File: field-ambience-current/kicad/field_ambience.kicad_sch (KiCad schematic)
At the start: 0 parts

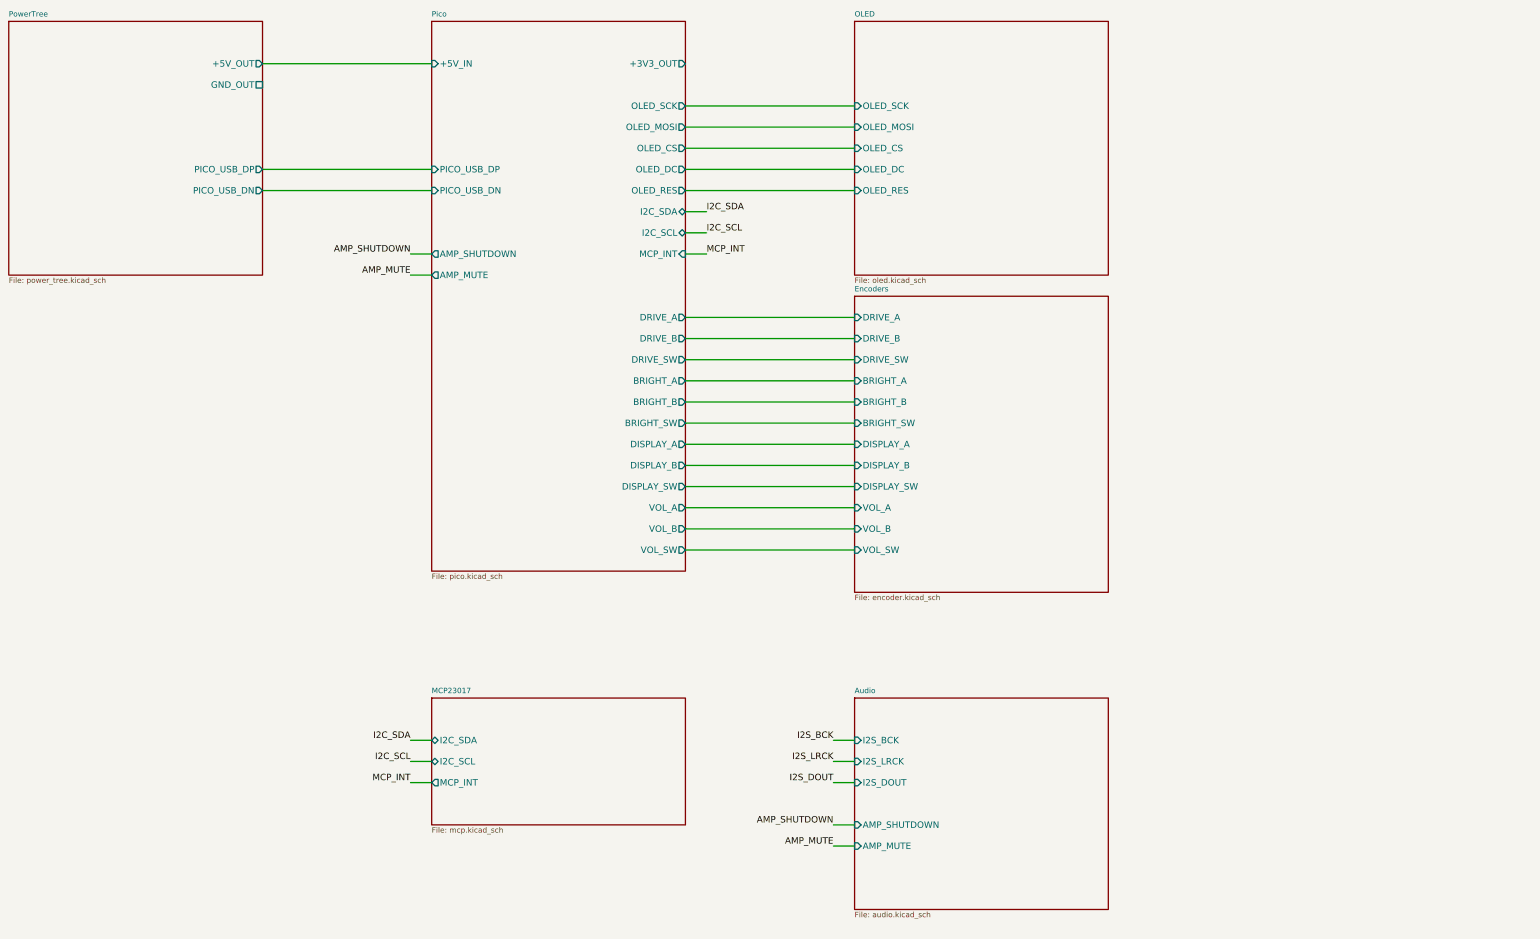
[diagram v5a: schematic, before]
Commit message: Add Sheet 7 (Pi Zero 2 W GPIO Header) per SPEC v0.6 §1/§8
J2 2x20 GPIO Header für Pi Zero 2 W:
- Pin 2, 4: +5V Power-Injection (von unserer PCB-Rail zum Pi)
- Pin 6, 9, 14, 20, 25, 30, 34, 39: GND (8x Pi GND-Pins)
- Pin 1, 17: NC (Pi 3V3 output ungenutzt — unsere 3V3 kommt vom Pico SMPS)

UART (115200) Pi ↔ Pico:
- Pin 10 (Pi GPIO15 RX) ← UART0_TX (von Pico GP0 direkt)
- Pin 8 (Pi GPIO14 TX) → R1 1k series → UART0_RX (zu Pico GP1, per SPEC v0.6 §5 BOM)

I²S Audio Pi → PCM5102A:
- Pin 12 (Pi GPIO18 PCM_CLK) → I2S_BCK
- Pin 35 (Pi GPIO19 PCM_FS) → I2S_LRCK
- Pin 40 (Pi GPIO21 PCM_DOUT) → I2S_DOUT

Alle 23 ungenutzten GPIOs (3, 5, 7, 11, 13, 15, 16, 18, 19, 21-24, 26-29,
31-33, 36-38) als NC-Labels mit informativen Namen markiert
(NC_GPIO2_SDA1, NC_GPIO10_MOSI, etc).

Root sheet: Pi-Sheet bei (330, 40) size (60, 130) mit 5 sheet-pins.
Pico-Sheet bekommt UART0_TX (output) + UART0_RX (input) auf linker Seite.
Label-bridges für UART (Pico↔Pi) und I2S (Pi→Audio).

Conn_02x20 generic lib_symbol generator hinzugefügt (alternating
odd/even Pin-Numbering, 2.54mm spacing).

Analyzer: 0 functional errors (3 VM-001 false positives unverändert).
19 warnings (von 24 gefallen, UART/I2S jetzt closed loop). 83 components
total (28 caps, 24 resistors, 16 switches, 6 connectors, 4 ICs, 2 diodes,
1 fuse, 1 ferrite, 1 LED).

J2 pin_nets verifiziert: alle Power-Pins korrekt, alle GND-Pins korrekt,
UART/I2S-Verbindungen passen zum SPEC §8.

**Damit ist die KiCad-Schematic-Eingabe für SPEC v0.6 komplett.**
Next Steps: ERC clean in KiCad GUI, PCB-Layout, DRC, BOM, JLC-Order.
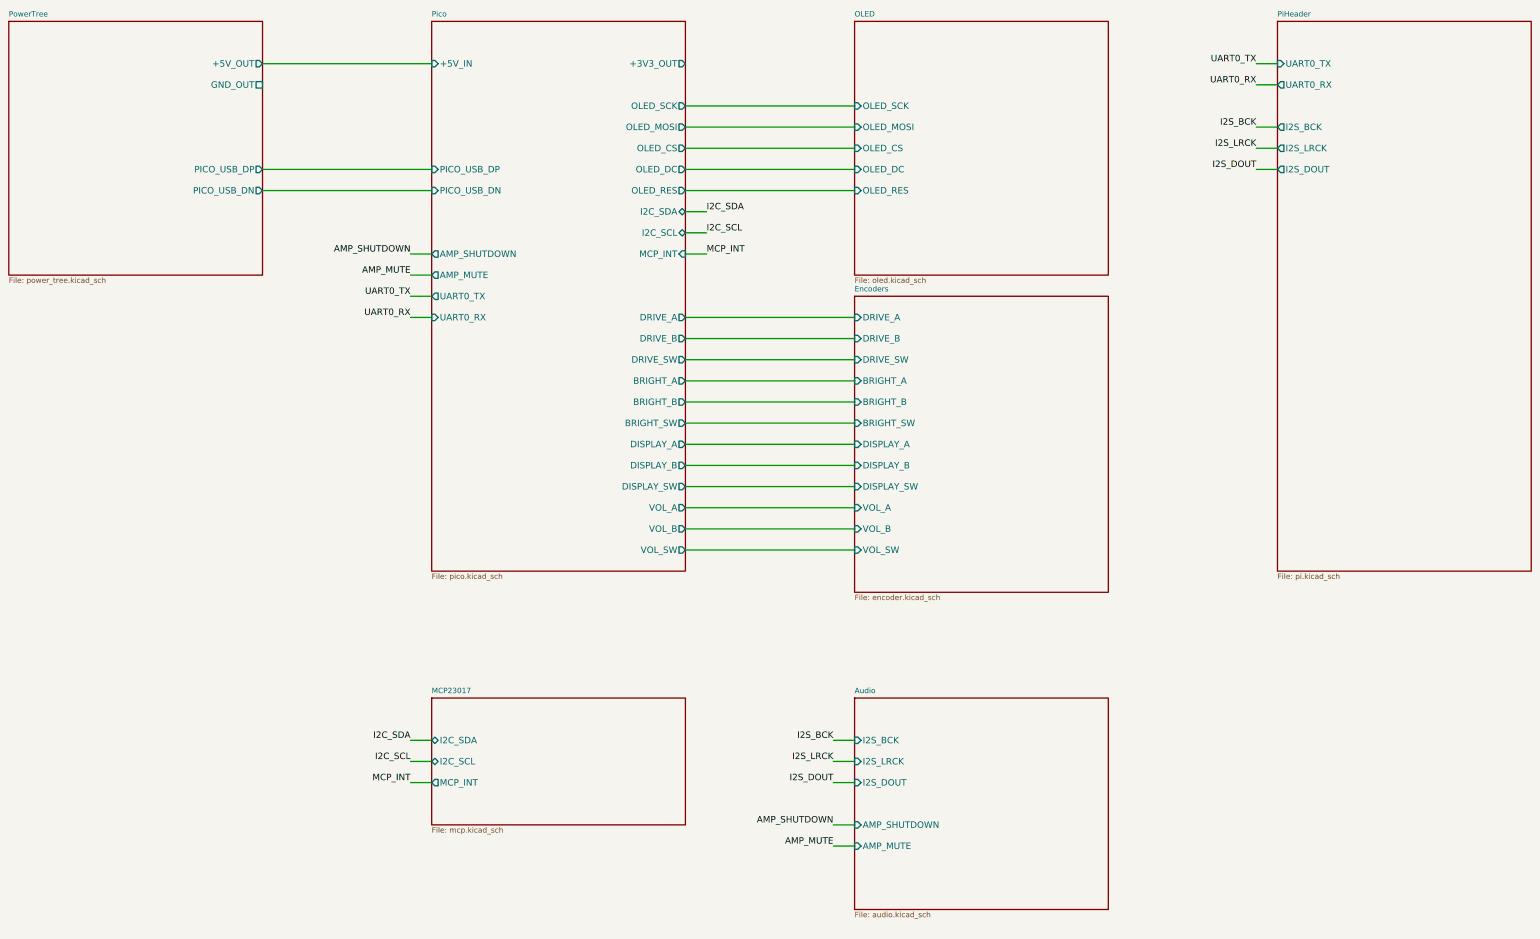
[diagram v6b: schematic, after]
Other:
- added sheet PiHeader (pi.kicad_sch)
- sheet Pico ports: added UART0_RX, UART0_TX; removed none
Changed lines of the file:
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@@
     (pin "AMP_MUTE" output (at 130 100 180)
+      (effects (font (size 1.524 1.524)) (justify left))
+)
+    (pin "UART0_TX" output (at 130 105 180)
+      (effects (font (size 1.524 1.524)) (justify left))
+)
+    (pin "UART0_RX" input (at 130 110 180)
       (effects (font (size 1.524 1.524)) (justify left))
 ))
@@
   (wire (pts (xy 125 220) (xy 130 220)) (stroke (width 0) (type default)))
   (label "MCP_INT" (at 125 220 0) (effects (font (size 1.524 1.524)) (justify right bottom)))
+  (sheet (at 330 40) (size 60 130) (fields_autoplaced)
+    (stroke (width 0.1524) (type solid))
+    (fill (color 0 0 0 0.0000))
+    (property "Sheetname" "PiHeader" (at 330 39 0)
+      (effects (font (size 1.27 1.27)) (justify left bottom)))
+    (property "Sheetfile" "pi.kicad_sch" (at 330 170.5 0)
+      (effects (font (size 1.27 1.27)) (justify left top)))
+    (pin "UART0_TX" input (at 330 50 180)
+      (effects (font (size 1.524 1.524)) (justify left))
+)
+    (pin "UART0_RX" output (at 330 55 180)
+      (effects (font (size 1.524 1.524)) (justify left))
+)
+    (pin "I2S_BCK" output (at 330 65 180)
+      (effects (font (size 1.524 1.524)) (justify left))
+)
+    (pin "I2S_LRCK" output (at 330 70 180)
+      (effects (font (size 1.524 1.524)) (justify left))
+)
+    (pin "I2S_DOUT" output (at 330 75 180)
+      (effects (font (size 1.524 1.524)) (justify left))
+))
+  (wire (pts (xy 125 105) (xy 130 105)) (stroke (width 0) (type default)))
+  (label "UART0_TX" (at 125 105 0) (effects (font (size 1.524 1.524)) (justify right bottom)))
+  (wire (pts (xy 125 110) (xy 130 110)) (stroke (width 0) (type default)))
+  (label "UART0_RX" (at 125 110 0) (effects (font (size 1.524 1.524)) (justify right bottom)))
+  (wire (pts (xy 325 50) (xy 330 50)) (stroke (width 0) (type default)))
+  (label "UART0_TX" (at 325 50 0) (effects (font (size 1.524 1.524)) (justify right bottom)))
+  (wire (pts (xy 325 55) (xy 330 55)) (stroke (width 0) (type default)))
+  (label "UART0_RX" (at 325 55 0) (effects (font (size 1.524 1.524)) (justify right bottom)))
+  (wire (pts (xy 325 65) (xy 330 65)) (stroke (width 0) (type default)))
+  (label "I2S_BCK" (at 325 65 0) (effects (font (size 1.524 1.524)) (justify right bottom)))
+  (wire (pts (xy 325 70) (xy 330 70)) (stroke (width 0) (type default)))
+  (label "I2S_LRCK" (at 325 70 0) (effects (font (size 1.524 1.524)) (justify right bottom)))
+  (wire (pts (xy 325 75) (xy 330 75)) (stroke (width 0) (type default)))
+  (label "I2S_DOUT" (at 325 75 0) (effects (font (size 1.524 1.524)) (justify right bottom)))
   (sheet (at 230 200) (size 60 50) (fields_autoplaced)
     (stroke (width 0.1524) (type solid))

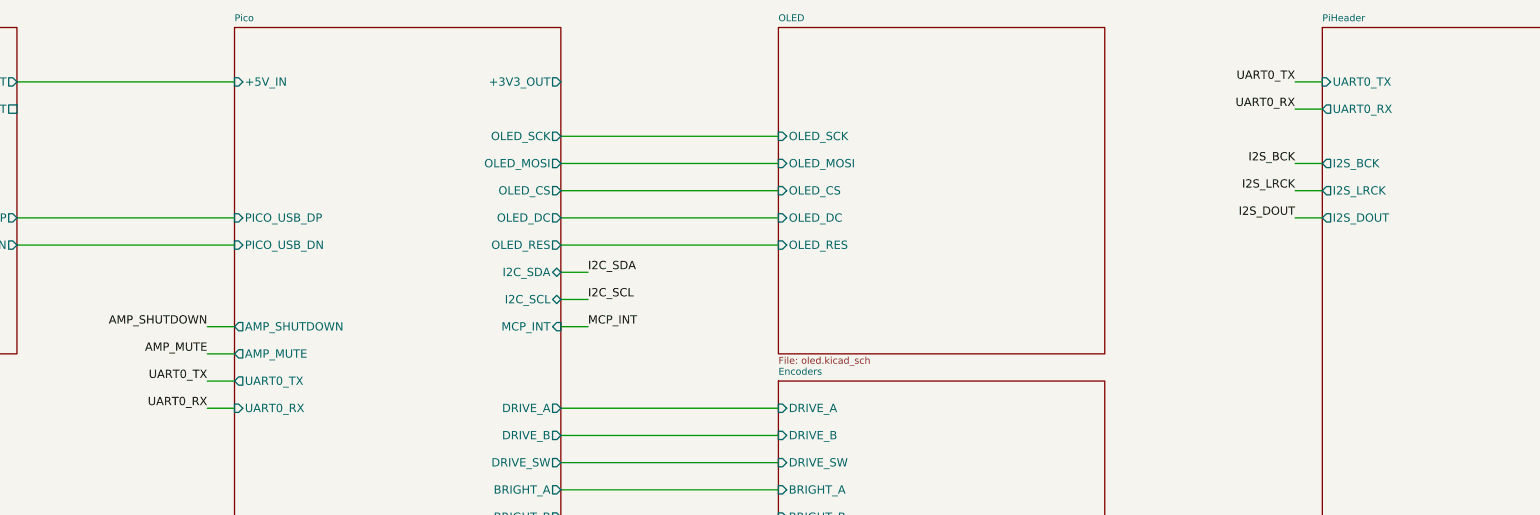
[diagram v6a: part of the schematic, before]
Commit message: v0.6.3-r2: PAM8403 SHDN/MUTE pull-downs + UART naming + TODO list
Addresses 2nd-iteration ChatGPT review findings (most that don't need
KiCad GUI). All TODO items documented in PCB_TODO.md.

B4: PAM8403H /SHDN and /MUTE hardware pull-downs
- R_MUTE_PD 10k from pin 5 (/MUTE) to GND
- R_SHDN_PD 10k from pin 12 (/SHDN) to GND
- Default state during Pico boot/reset = both LOW = Amp OFF + MUTED
- Pico firmware drives HIGH only after power-sequencing per SPEC §5
- Prevents undefined Amp state during boot transients (pop/click safety)

I7: UART net naming disambiguated
- Old: UART0_TX / UART0_RX (perspective-ambiguous)
- New:
  - PICO_TX_PI_RX (Pico GP0 → Pi GPIO15 pin 10)
  - PI_TX_PICO_RX (Pi GPIO14 pin 8 → R1 1k → Pico GP1)
- Changed in pico_sheet, pi_sheet, root_sheet (pins + labels)

N4: Titleblock revs synced
- audio.kicad_sch: v0.6.1 → v0.6.3
- power_tree.kicad_sch: v0.6 → v0.6.3
- Comments updated to reflect current state

N5: Stale comments cleanup
- power_tree_sheet: USB-C pin-number references updated to USB-C spec
- audio_sheet: PAM8403 references updated to PAM8403H + PDF reference
- BLOCKER-comment in audio sheet replaced with "boot-safe pull-downs added"

New PCB_TODO.md tracks remaining items for PCB-layout readiness:
- BLOCKER (4): need KiCad GUI — footprint verification, ERC report
- IMPORTANT (7): power budget recalc, mech coords, BOM split, etc.
- NICE-TO-HAVE (5): XSMT via GPIO, I²S series R, etc.

Analyzer status: 0 functional errors (same 3 VM-001 false positives),
19 warnings, 87 components (was 85, +2 for pull-downs), 117 nets.

Verified via analyzer pin_nets:
- R_MUTE_PD: pin1=AMP_MUTE, pin2=GND ✓
- R_SHDN_PD: pin1=AMP_SHUTDOWN, pin2=GND ✓
- U1 Pin 1 (GP0) = PICO_TX_PI_RX ✓
- U1 Pin 2 (GP1) = PI_TX_PICO_RX ✓
- U4 Pin 5 (MUTE) = AMP_MUTE ✓
- U4 Pin 12 (SHDN) = AMP_SHUTDOWN ✓

Note on reviewer's USB-C claim: Reviewer indicated USB-C symbol still
has wrong pinout in PR. Verified via GitHub API that PR HEAD (commit
5ca0bcb) has the correct mapping (VB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
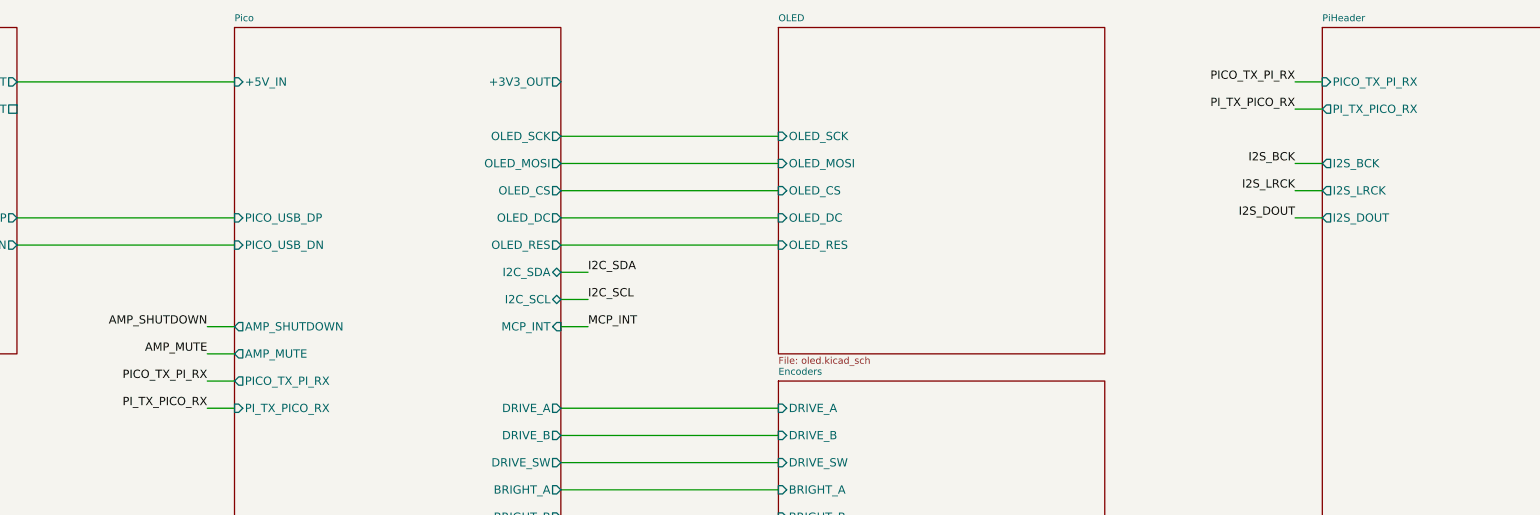
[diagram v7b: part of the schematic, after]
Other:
- sheet PiHeader ports: added PICO_TX_PI_RX, PI_TX_PICO_RX; removed UART0_RX, UART0_TX
- sheet Pico ports: added PICO_TX_PI_RX, PI_TX_PICO_RX; removed UART0_RX, UART0_TX
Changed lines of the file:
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@@
       (effects (font (size 1.524 1.524)) (justify left))
 )
-    (pin "UART0_TX" output (at 130 105 180)
+    (pin "PICO_TX_PI_RX" output (at 130 105 180)
       (effects (font (size 1.524 1.524)) (justify left))
 )
-    (pin "UART0_RX" input (at 130 110 180)
+    (pin "PI_TX_PICO_RX" input (at 130 110 180)
       (effects (font (size 1.524 1.524)) (justify left))
 ))
@@
     (property "Sheetfile" "pi.kicad_sch" (at 330 170.5 0)
       (effects (font (size 1.27 1.27)) (justify left top)))
-    (pin "UART0_TX" input (at 330 50 180)
+    (pin "PICO_TX_PI_RX" input (at 330 50 180)
       (effects (font (size 1.524 1.524)) (justify left))
 )
-    (pin "UART0_RX" output (at 330 55 180)
+    (pin "PI_TX_PICO_RX" output (at 330 55 180)
       (effects (font (size 1.524 1.524)) (justify left))
 )
@@
 ))
   (wire (pts (xy 125 105) (xy 130 105)) (stroke (width 0) (type default)))
-  (label "UART0_TX" (at 125 105 0) (effects (font (size 1.524 1.524)) (justify right bottom)))
+  (label "PICO_TX_PI_RX" (at 125 105 0) (effects (font (size 1.524 1.524)) (justify right bottom)))
   (wire (pts (xy 125 110) (xy 130 110)) (stroke (width 0) (type default)))
-  (label "UART0_RX" (at 125 110 0) (effects (font (size 1.524 1.524)) (justify right bottom)))
+  (label "PI_TX_PICO_RX" (at 125 110 0) (effects (font (size 1.524 1.524)) (justify right bottom)))
   (wire (pts (xy 325 50) (xy 330 50)) (stroke (width 0) (type default)))
-  (label "UART0_TX" (at 325 50 0) (effects (font (size 1.524 1.524)) (justify right bottom)))
+  (label "PICO_TX_PI_RX" (at 325 50 0) (effects (font (size 1.524 1.524)) (justify right bottom)))
   (wire (pts (xy 325 55) (xy 330 55)) (stroke (width 0) (type default)))
-  (label "UART0_RX" (at 325 55 0) (effects (font (size 1.524 1.524)) (justify right bottom)))
+  (label "PI_TX_PICO_RX" (at 325 55 0) (effects (font (size 1.524 1.524)) (justify right bottom)))
   (wire (pts (xy 325 65) (xy 330 65)) (stroke (width 0) (type default)))
   (label "I2S_BCK" (at 325 65 0) (effects (font (size 1.524 1.524)) (justify right bottom)))
